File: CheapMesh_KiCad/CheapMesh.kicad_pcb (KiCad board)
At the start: 2 copper layers, 34.8 x 67.3 mm, 24 parts, among them J1 Conn_01x02_Pin, J2 Conn_01x09_Pin, J3 USB_A, J4 USB_C, J5 Conn_Coaxial, Q1 UMH3N, U1 L78L33, U2 HT-CT62, U3 AP2112K-3.3

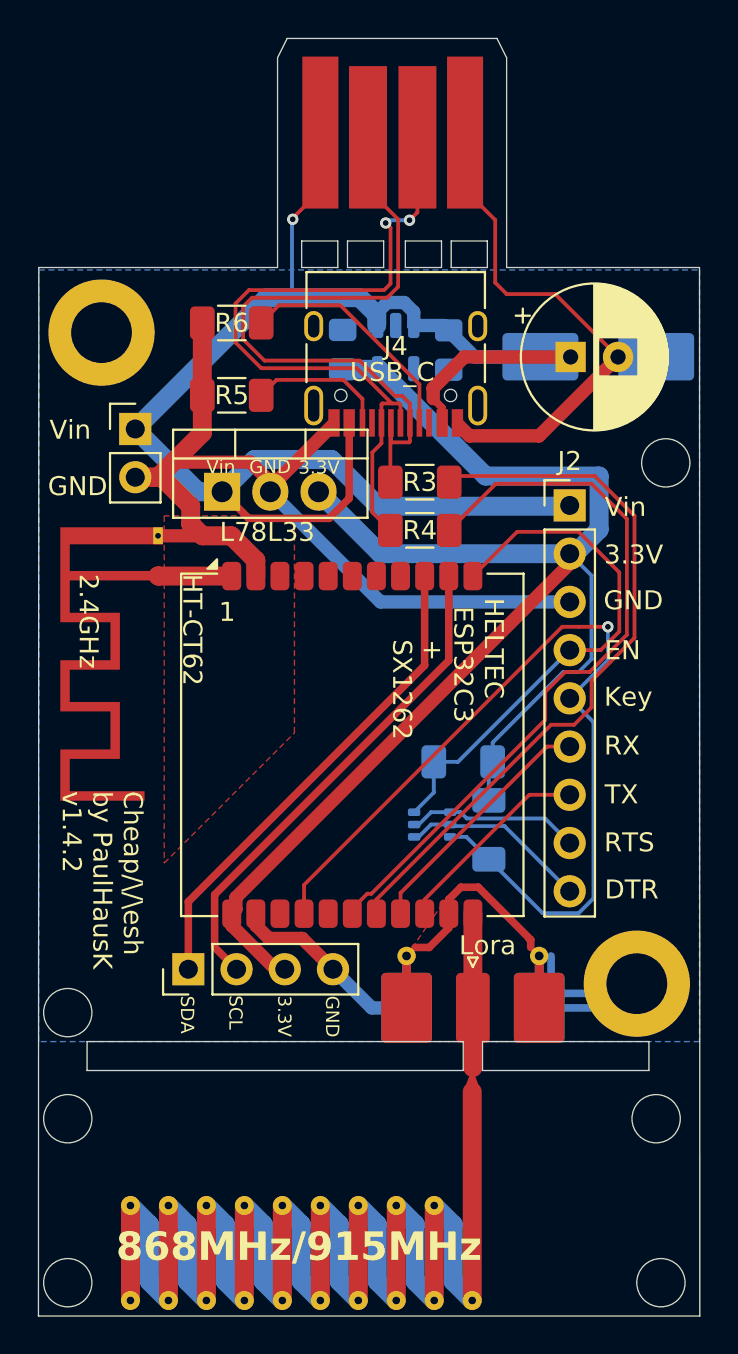
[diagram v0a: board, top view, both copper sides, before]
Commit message: update
swapp d+ d-, add gpio 2, PCB v 1.4.4
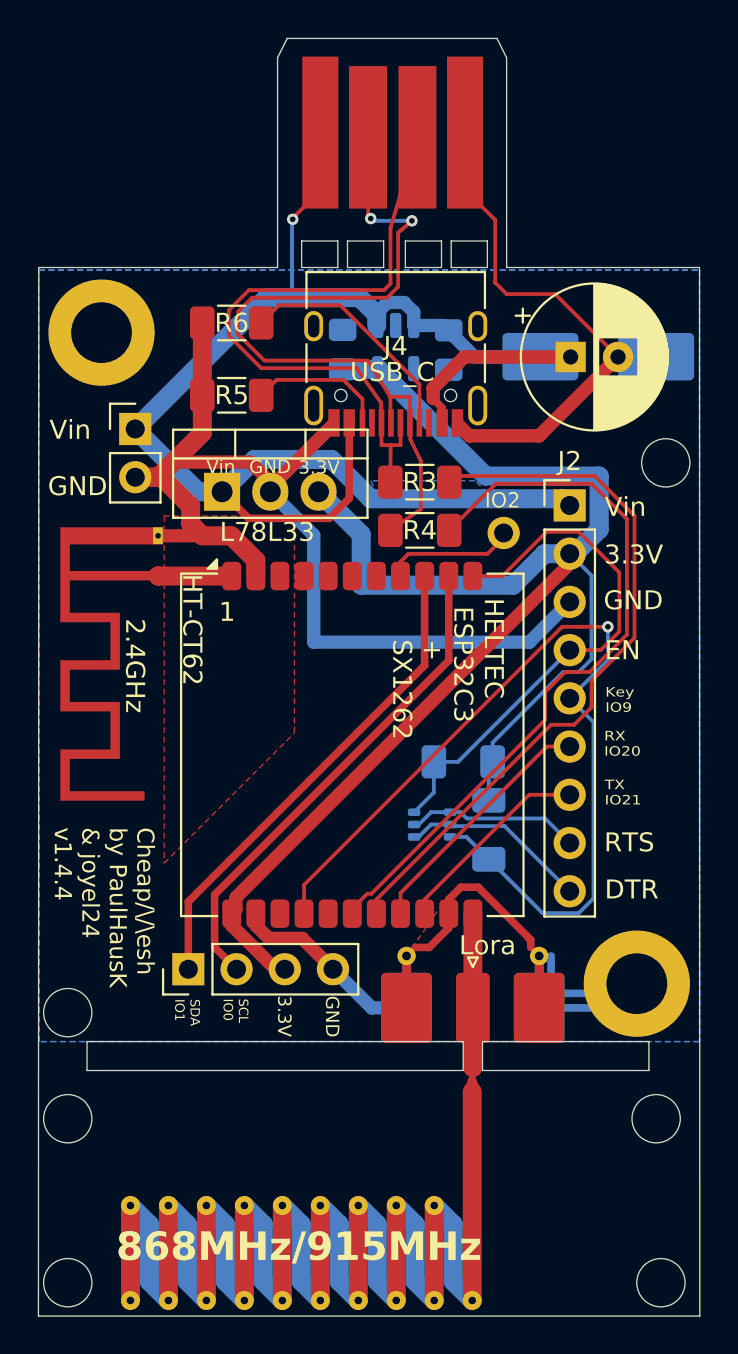
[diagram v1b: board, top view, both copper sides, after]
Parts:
- added ?: , , F.Cu at (57.5, 134.2)
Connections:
- R3 pad 1: Net-(J3-D-) -> Net-(J3-D+)
- R3 pad 2: USB_D- -> USB_D+
- R4 pad 1: Net-(J3-D+) -> Net-(J3-D-)
- R4 pad 2: USB_D+ -> USB_D-
- U2 pad 17: USB_D+ -> USB_D-
- U2 pad 18: USB_D- -> USB_D+
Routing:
- net Net-(J3-D-): track 34.0 -> 42.7 mm, vias 0 -> 2
- net unconnected-(U2-GPIO2-Pad8): track 0.00 -> 6.71 mm
- net GND: track 127.1 -> 132.2 mm
- net Net-(J3-D+): track 38.6 -> 34.4 mm, vias 2 -> 0
- net 3.3V: track 83.2 -> 86.1 mm
- net USB_D-: track 38.1 -> 39.1 mm
- net USB_D+: track 39.1 -> 38.1 mm
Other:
- board text added: "Cheap/\/\esh by PaulHausK & joyel24 v1.4.4"
- board text added: "IO2"
- board text added: "Key IO9"
- board text added: "RX IO20"
- board text added: "SCL IO0"
- board text added: "SDA IO1"
- board text added: "TX IO21"
- board text removed: "Cheap/\/\esh by PaulHausK v1.4.2"
- board text removed: "Key"
- board text removed: "RX"
- board text removed: "SCL"
- board text removed: "SDA"
- board text removed: "TX"
